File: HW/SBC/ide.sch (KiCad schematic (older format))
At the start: 0 parts

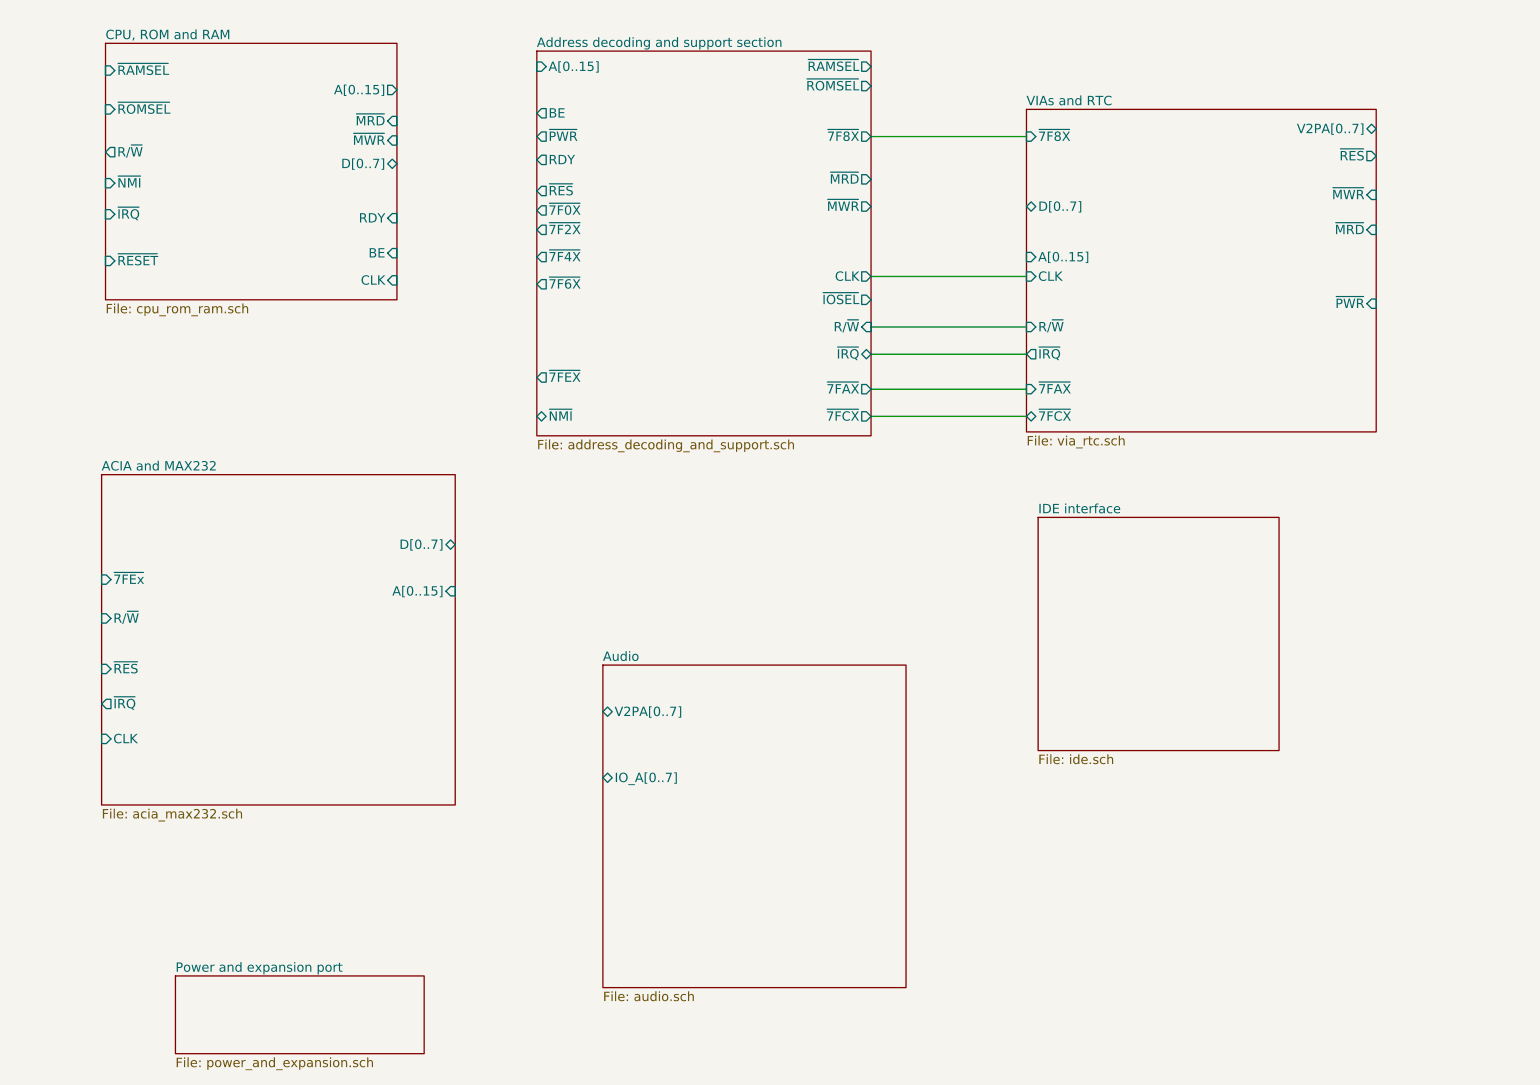
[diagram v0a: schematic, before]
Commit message: Moved IDE schematics (WIP) into pluto.
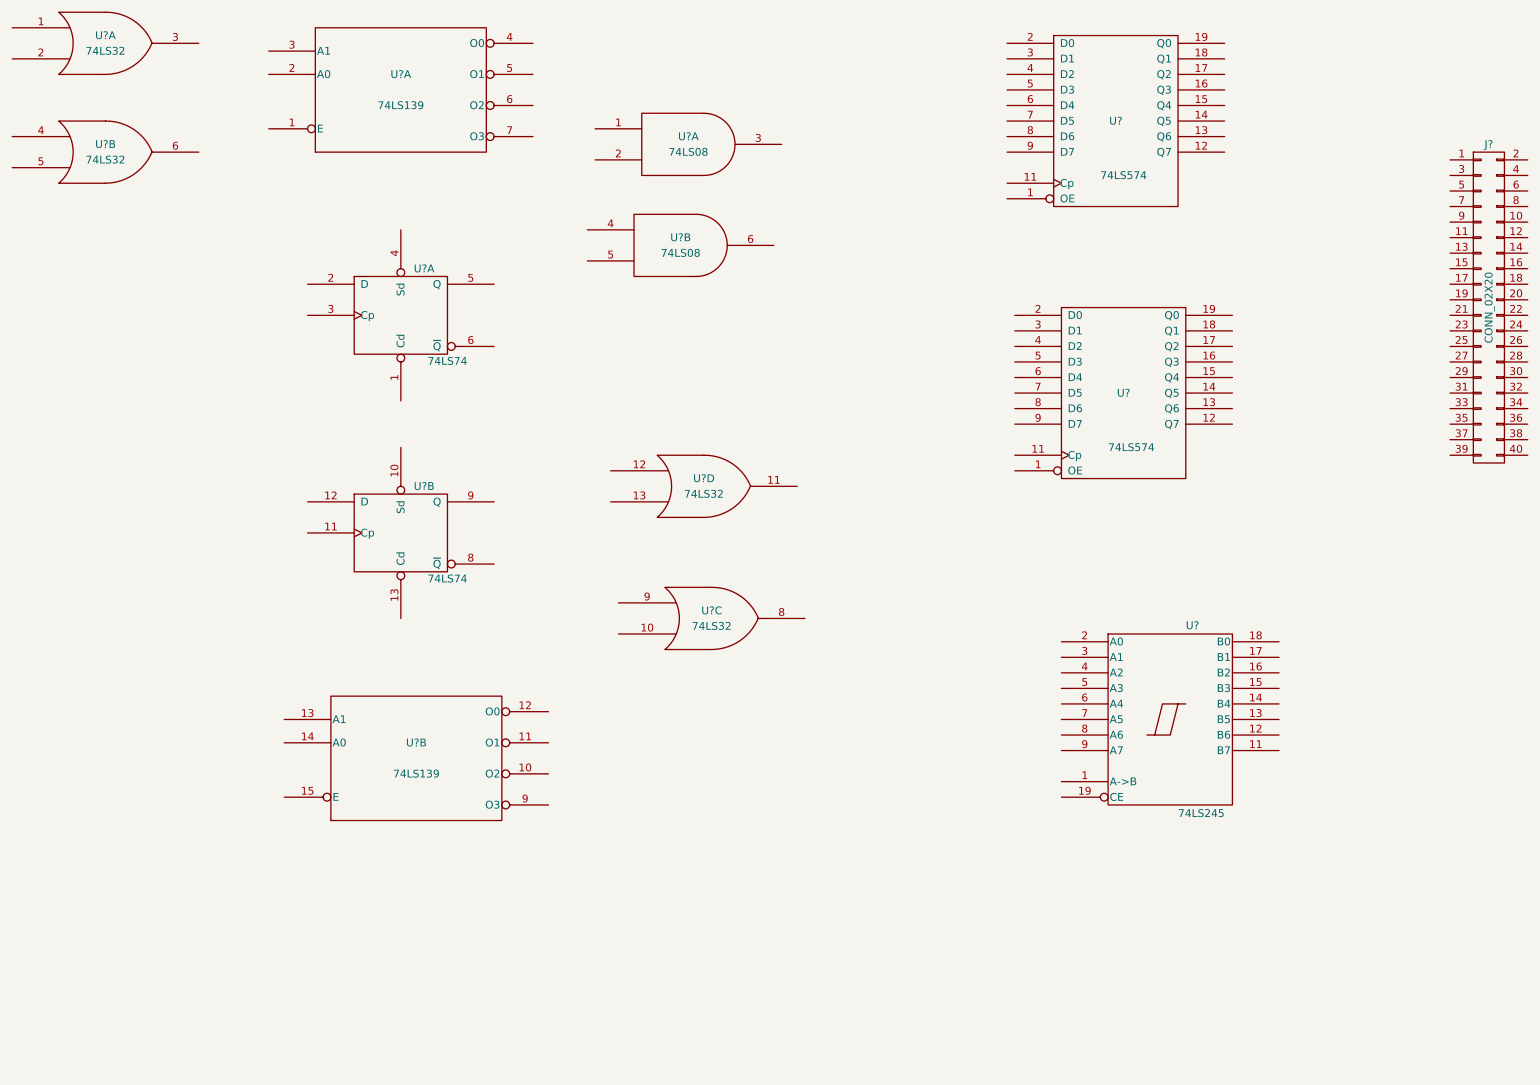
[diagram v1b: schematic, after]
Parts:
- added J?: CONN_02X20, symbol CONN_02X20
- added U?: 74LS245, symbol 74LS245
- added U? (x4): 74LS32, symbol 74LS32
- added U? (x2): 74LS74, symbol 74LS74
- added U? (x2): 74LS139, symbol 74LS139
- added U? (x2): 74LS08, symbol 74LS08
- added U? (x2): 74LS574, symbol 74LS574
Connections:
- new net GND: U?.10 (GND), U?.10 (GND), U?.10 (GND), U?.7 (GND), U?.7 (GND), U?.7 (GND), U?.7 (GND), U?.7 (GND), U?.7 (GND), U?.7 (GND), U?.7 (GND), U?.8 (GND), U?.8 (GND)
- new net VCC: U?.14 (VCC), U?.14 (VCC), U?.14 (VCC), U?.14 (VCC), U?.14 (VCC), U?.14 (VCC), U?.14 (VCC), U?.14 (VCC), U?.16 (VCC), U?.16 (VCC), U?.20 (VCC), U?.20 (VCC), U?.20 (VCC)
